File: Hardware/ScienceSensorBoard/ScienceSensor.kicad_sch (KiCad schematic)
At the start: 93 parts, among them J1 Conn_02x03_Counter_Clockwise, J2 RJ45_LED_Shielded, Q1 SI4156DY, Q10 BSS138, Q11 SI4156DY, Q2 SI4156DY, Q3 SI4156DY, Q4 BSS138, Q5 BSS138, Q6 BSS138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

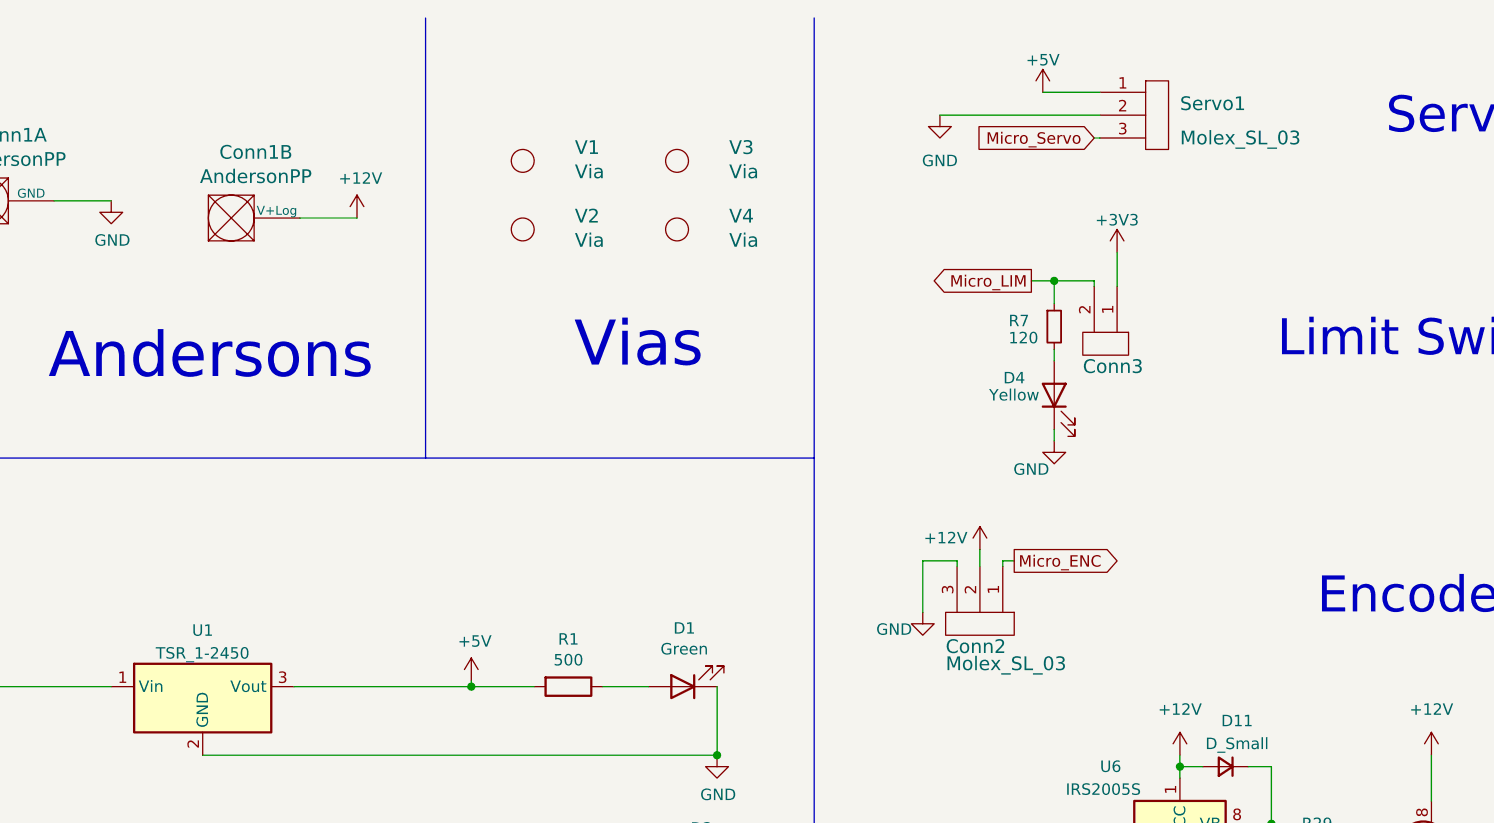
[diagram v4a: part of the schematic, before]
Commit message: Fixing ERC errors, Updated BOM
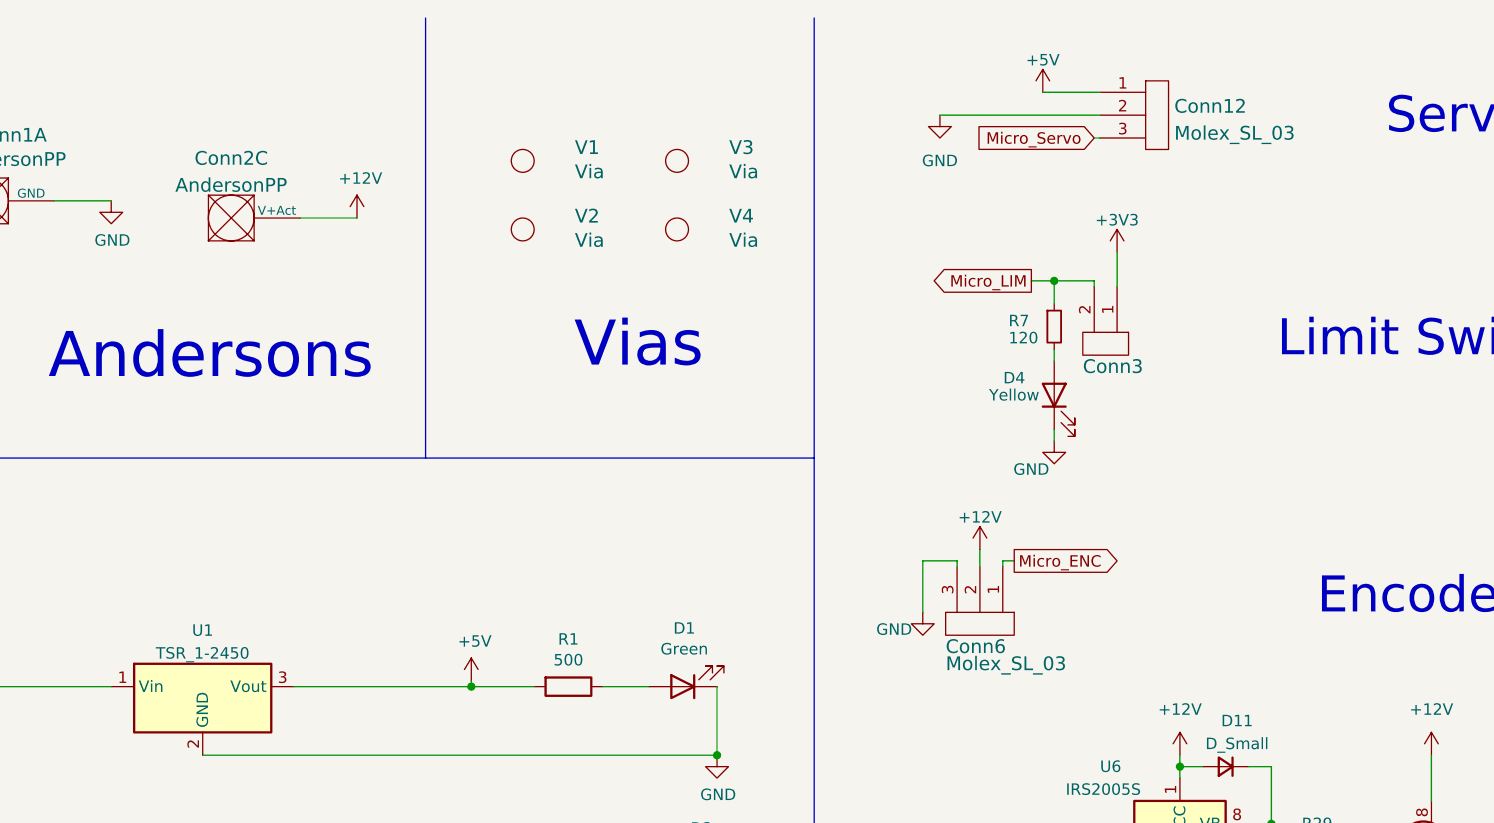
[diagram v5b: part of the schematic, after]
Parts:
- removed unit 2 of Conn1
- added Conn2: AndersonPP, symbol MRDT_Connectors:AndersonPP
- renumbered Servo1 to Conn12, Conn2 to Conn6
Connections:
- net +12V: now also Conn6.2, Conn2.3 (V+Act)
- net +3V3: no longer Conn6.2
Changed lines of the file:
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@@
   (junction (at 254 101.6) (diameter 0) (color 0 0 0 0)
   )
-  (junction (at 264.16 95.25) (diameter 0) (color 0 0 0 0)
-  )
   (junction (at 270.51 217.17) (diameter 0) (color 0 0 0 0)
   )
@@
   (junction (at 216.535 273.685) (diameter 0) (color 0 0 0 0)
   )
+  (junction (at 264.16 95.25) (diameter 0) (color 0 0 0 0)
+  )
   (junction (at 162.56 114.3) (diameter 0) (color 0 0 0 0)
   )
@@
     (stroke (width 0) (type default) (color 0 0 0 0))
   )
+  (wire (pts (xy 264.16 95.25) (xy 264.16 96.52))
+    (stroke (width 0) (type default) (color 0 0 0 0))
+  )
   (wire (pts (xy 53.975 86.36) (xy 73.66 86.36))
     (stroke (width 0) (type default) (color 0 0 0 0))
@@
     (stroke (width 0) (type default) (color 0 0 0 0))
   )
-  (wire (pts (xy 264.16 93.98) (xy 264.16 95.25))
-    (stroke (width 0) (type default) (color 0 0 0 0))
-  )
   (wire (pts (xy 45.085 116.205) (xy 63.5 116.205))
     (stroke (width 0) (type default) (color 0 0 0 0))
@@
     (stroke (width 0) (type default) (color 0 0 0 0))
   )
-  (wire (pts (xy 261.62 95.25) (xy 264.16 95.25))
-    (stroke (width 0) (type default) (color 0 0 0 0))
-  )
   (wire (pts (xy 351.155 156.845) (xy 352.425 156.845))
     (stroke (width 0) (type default) (color 0 0 0 0))
@@
     (stroke (width 0) (type default) (color 0 0 0 0))
   )
+  (wire (pts (xy 264.16 93.98) (xy 264.16 95.25))
+    (stroke (width 0) (type default) (color 0 0 0 0))
+  )
   (wire (pts (xy 277.495 37.465) (xy 277.495 36.83))
     (stroke (width 0) (type default) (color 0 0 0 0))
@@
     (stroke (width 0) (type default) (color 0 0 0 0))
   )
+  (wire (pts (xy 261.62 95.25) (xy 264.16 95.25))
+    (stroke (width 0) (type default) (color 0 0 0 0))
+  )
   (wire (pts (xy 251.46 214.63) (xy 251.46 217.17))
     (stroke (width 0) (type default) (color 0 0 0 0))
@@
     (stroke (width 0) (type default) (color 0 0 0 0))
   )
-  (wire (pts (xy 130.175 71.12) (xy 130.175 73.025))
-    (stroke (width 0) (type default) (color 0 0 0 0))
-  )
   (wire (pts (xy 254 101.6) (xy 254 95.25))
     (stroke (width 0) (type default) (color 0 0 0 0))
@@
     (stroke (width 0) (type default) (color 0 0 0 0))
   )
+  (wire (pts (xy 130.175 71.12) (xy 130.175 73.025))
+    (stroke (width 0) (type default) (color 0 0 0 0))
+  )
   (wire (pts (xy 180.34 109.22) (xy 180.34 110.49))
     (stroke (width 0) (type default) (color 0 0 0 0))
@@
     (stroke (width 0) (type default) (color 0 0 0 0))
   )
-  (wire (pts (xy 264.16 95.25) (xy 264.16 96.52))
-    (stroke (width 0) (type default) (color 0 0 0 0))
-  )
   (wire (pts (xy 97.155 189.23) (xy 97.155 193.04))
     (stroke (width 0) (type default) (color 0 0 0 0))
@@
     (pin "1")
   )
-  (symbol (lib_id "MRDT_Connectors:AndersonPP") (at 44.45 36.83 0) (unit 2)
-    (in_bom yes) (on_board yes)
-    (property "Reference" "Conn1" (id 0) (at 49.7332 27.0002 0)
-      (effects (font (size 1.524 1.524)))
-    )
-    (property "Value" "AndersonPP" (id 1) (at 49.7332 29.6926 0)
-      (effects (font (size 1.524 1.524)))
-    )
-    (property "Footprint" "" (id 2) (at 40.64 50.8 0)
-      (effects (font (size 1.524 1.524)) hide)
-    )
-    (property "Datasheet" "" (id 3) (at 40.64 50.8 0)
-      (effects (font (size 1.524 1.524)) hide)
-    )
-    (pin "1")
-    (pin "2")
-    (pin "3")
-    (pin "4")
-    (pin "1")
-  )
   (symbol (lib_id "power:+5V") (at 73.66 85.725 0) (unit 1)
     (in_bom yes) (on_board yes)
@@
     (pin "VUSB")
   )
-  (symbol (lib_id "ArmBoard_Hardware-rescue:+3.3V-power") (at 130.175 71.12 0) (unit 1)
-    (in_bom yes) (on_board yes)
-    (property "Reference" "#PWR015" (id 0) (at 130.175 74.93 0)
-      (effects (font (size 1.27 1.27)) hide)
-    )
-    (property "Value" "+12V" (id 1) (at 126.365 69.85 0))
-    (property "Footprint" "" (id 2) (at 130.175 71.12 0)
-      (effects (font (size 1.27 1.27)) hide)
-    )
-    (property "Datasheet" "" (id 3) (at 130.175 71.12 0)
-      (effects (font (size 1.27 1.27)) hide)
-    )
-    (pin "1")
-  )
   (symbol (lib_id "power:+5V") (at 370.205 55.245 0) (unit 1)
     (in_bom yes) (on_board yes)
@@
     (pin "1")
   )
+  (symbol (lib_id "power:+12V") (at 130.175 71.12 0) (unit 1)
+    (in_bom yes) (on_board yes) (fields_autoplaced)
+    (property "Reference" "#PWR0101" (id 0) (at 130.175 74.93 0)
+      (effects (font (size 1.27 1.27)) hide)
+    )
+    (property "Value" "+12V" (id 1) (at 130.175 67.5442 0))
+    (property "Footprint" "" (id 2) (at 130.175 71.12 0)
+      (effects (font (size 1.27 1.27)) hide)
+    )
+    (property "Datasheet" "" (id 3) (at 130.175 71.12 0)
+      (effects (font (size 1.27 1.27)) hide)
+    )
+    (pin "1")
+  )
   (symbol (lib_id "MRDT_Connectors:Molex_SL_03") (at 126.365 78.105 270) (unit 1)
     (in_bom yes) (on_board yes)
-    (property "Reference" "Conn2" (id 0) (at 126.365 81.915 90)
+    (property "Reference" "Conn6" (id 0) (at 126.365 81.915 90)
       (effects (font (size 1.524 1.524)) (justify left))
     )
@@
     (pin "2")
   )
+  (symbol (lib_id "MRDT_Connectors:AndersonPP") (at 44.45 36.83 0) (unit 3)
+    (in_bom yes) (on_board yes) (fields_autoplaced)
+    (property "Reference" "Conn2" (id 0) (at 46.99 27.6659 0)
+      (effects (font (size 1.524 1.524)))
+    )
+    (property "Value" "AndersonPP" (id 1) (at 46.99 30.6593 0)
+      (effects (font (size 1.524 1.524)))
+    )
+    (property "Footprint" "" (id 2) (at 40.64 50.8 0)
+      (effects (font (size 1.524 1.524)) hide)
+    )
+    (property "Datasheet" "" (id 3) (at 40.64 50.8 0)
+      (effects (font (size 1.524 1.524)) hide)
+    )
+    (pin "1")
+    (pin "2")
+    (pin "3")
+    (pin "4")
+    (pin "1")
+  )
   (symbol (lib_id "power:+5V") (at 81.28 179.07 0) (unit 1)
     (in_bom yes) (on_board yes)
@@
   (symbol (lib_id "MRDT_Connectors:Molex_SL_03") (at 148.59 26.67 0) (unit 1)
     (in_bom yes) (on_board yes) (fields_autoplaced)
-    (property "Reference" "Servo1" (id 0) (at 152.4 21.59 0)
+    (property "Reference" "Conn12" (id 0) (at 151.765 21.8838 0)
       (effects (font (size 1.524 1.524)) (justify left))
     )
-    (property "Value" "Molex_SL_03" (id 1) (at 152.4 25.4 0)
+    (property "Value" "Molex_SL_03" (id 1) (at 151.765 24.8772 0)
       (effects (font (size 1.524 1.524)) (justify left))
     )
@@
       (reference "#PWR014") (unit 1) (value "GND") (footprint "")
     )
-    (path "/2fa72ae1-4629-4bfe-ba46-42c110783f4a"
-      (reference "#PWR015") (unit 1) (value "+12V") (footprint "")
-    )
     (path "/2cd81dea-5dd1-45c5-97bb-42b6bc72e149"
       (reference "#PWR016") (unit 1) (value "+5V") (footprint "")
@@
       (reference "#PWR067") (unit 1) (value "GND") (footprint "")
     )
+    (path "/49671190-4e1a-4b03-a0e9-4da1774c1d67"
+      (reference "#PWR0101") (unit 1) (value "+12V") (footprint "")
+    )
     (path "/7becaed6-99a4-49f3-99dd-3fce229dac4a"
       (reference "C1") (unit 1) (value "0.1uF") (footprint "Capacitor_SMD:C_0603_1608Metric_Pad1.08x0.95mm_HandSolder")
@@
       (reference "Conn1") (unit 1) (value "AndersonPP") (footprint "")
     )
-    (path "/00000000-0000-0000-0000-000063214fb6"
-      (reference "Conn1") (unit 2) (value "AndersonPP") (footprint "")
-    )
-    (path "/514d1d3a-5e7e-4cdf-800d-dc9fd4979572"
-      (reference "Conn2") (unit 1) (value "Molex_SL_03") (footprint "MRDT_Connectors:MOLEX_SL_03_Vertical")
+    (path "/7095feda-30c9-4bfd-9ce4-1857ac5357e8"
+      (reference "Conn2") (unit 3) (value "AndersonPP") (footprint "")
     )
     (path "/362043ba-7077-4355-842f-ed4e21c764a7"
@@
       (reference "Conn5") (unit 2) (value "AndersonPP") (footprint "MRDT_Connectors:Anderson_2_Horizontal_Side_by_Side")
     )
+    (path "/514d1d3a-5e7e-4cdf-800d-dc9fd4979572"
+      (reference "Conn6") (unit 1) (value "Molex_SL_03") (footprint "MRDT_Connectors:MOLEX_SL_03_Vertical")
+    )
     (path "/0801cfcf-c1b0-4c18-945f-084fcc49db23"
       (reference "Conn7") (unit 1) (value "Molex_SL_03") (footprint "")
@@
       (reference "Conn11") (unit 1) (value "Molex_SL_04") (footprint "MRDT_Connectors:MOLEX_SL_04_Horizontal")
     )
+    (path "/c7884a03-c37f-45a7-baa0-a34c76a7670d"
+      (reference "Conn12") (unit 1) (value "Molex_SL_03") (footprint "")
+    )
     (path "/00000000-0000-0000-0000-000063231caf"
       (reference "D1") (unit 1) (value "Green") (footprint "")
@@
       (reference "R34") (unit 1) (value "100") (footprint "Resistor_SMD:R_0603_1608Metric_Pad0.98x0.95mm_HandSolder")
     )
-    (path "/c7884a03-c37f-45a7-baa0-a34c76a7670d"
-      (reference "Servo1") (unit 1) (value "Molex_SL_03") (footprint "")
-    )
     (path "/c5bc5e0f-59b7-45b6-b17c-1888cdf8bc2c"

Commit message: LED breakout, sensor changes
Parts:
- removed C3, C6: 2.2uF, Capacitor_SMD:C_0603_1608Metric_Pad1.08x0.95mm_HandSolder, symbol Device:C
- removed C5, C7: 3.3nF, Capacitor_SMD:C_0603_1608Metric_Pad1.08x0.95mm_HandSolder, symbol Device:C
- removed Conn11: Molex_SL_04, MRDT_Connectors:MOLEX_SL_04_Horizontal, symbol MRDT_Connectors:Molex_SL_04
- removed Conn4: Molex_SL_05, symbol MRDT_Connectors:Molex_SL_05
- removed R20, R26: 56k, Resistor_SMD:R_0603_1608Metric_Pad0.98x0.95mm_HandSolder, symbol Device:R
- removed R21, R27: 1M, Resistor_SMD:R_0603_1608Metric_Pad0.98x0.95mm_HandSolder, symbol Device:R
- removed U4, U5: TSV911RILT, Package_TO_SOT_SMD:SOT-23-5, symbol Amplifier_Operational:TSV911RILT
- added Conn4: Molex_SL_07, symbol MRDT_Connectors:Molex_SL_07
- added Conn?: Molex_SL_04, symbol MRDT_Connectors:Molex_SL_04
- added D? (x3): Blue, symbol Device:LED
- added R?: 100, symbol Device:R
- added R? (x2): 500, symbol Device:R
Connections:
- net +12V: now also Conn4.1
- net +5V: now also Conn4.2, Conn?.1
- net GND: now also Conn4.3, Conn?.2, D?.1 (K), D?.1 (K), D?.1 (K)
- net LED_315: now reaches U3.17 (A3)
- net LED_315: now also Conn4.7, R?.2
- net CH4_TX: now reaches U3.28 (RX7)
- net CH4_TX: now also Conn?.3, R?.2
- net CH4_RX: now reaches U3.29 (TX7)
- net CH4_RX: now also Conn?.4, R?.2
- net LED_1 renamed LED_260
- net LED_260: now also Conn4.4
- net LED_2 renamed LED_275
- net LED_275: now also Conn4.5
- net LED_3 renamed LED_280
- net LED_280: now also Conn4.6
- net NO_Gas: no longer names the net of U3.41 (A17)
- net NO_Ref: no longer names the net of U3.40 (A16)
- new net: D?.2 (A), R?.1 (x3)
- no-connect marks 41 -> 40
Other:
- note added: "CH4_Sensor"
- note removed: "NO_Sensor"
- moved on the sheet: Conn10, Conn8, Conn9, D10, D3, D5, D6, D7, D8, D9, Q7, R12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

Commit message: NH3, LED Mosfets
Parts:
- added Conn?: Molex_SL_04, symbol MRDT_Connectors:Molex_SL_04
- added R?: 820, symbol Device:R
- added R?: 93.1, symbol Device:R
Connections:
- net +5V: now also Conn?.1, Conn?.2; no longer Conn4.2
- net GND: now also Conn4.2, R?.1, R?.1; no longer Conn4.3
- net Micro_ENC: now also U3.40 (A16); no longer U3.27 (A13)
- net Micro_FWD: now also U3.38 (A14); no longer U3.25 (A11)
- net Micro_LIM: now also U3.41 (A17); no longer U3.38 (A14)
- net Micro_RVS: now also U3.27 (A13); no longer U3.24 (A10)
- net Micro_Servo: now also U3.39 (A15); no longer U3.26 (A12)
- net Photodiode_1: no longer U3.23 (A9)
- net NH3: now reaches U3.22 (A8)
- net NH3: now also Conn?.4, R?.2
- new net: Conn?.3, R?.2
- new net Photodiode_260: U3.26 (A12)
- new net Photodiode_275: U3.25 (A11)
- new net Photodiode_280: U3.24 (A10)
- new net Photodiode_315: U3.23 (A9)
- no-connect marks 40 -> 37
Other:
- note added: "NH3_Sensor"

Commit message: Footprint Assignment
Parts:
- added R36: 330, Resistor_SMD:R_0603_1608Metric_Pad0.98x0.95mm_HandSolder, symbol Device:R
- C10, C8: footprint Capacitor_SMD:C_0603_1608Metric -> Capacitor_SMD:C_0603_1608Metric_Pad1.08x0.95mm_HandSolder
- C2, C4, C9: footprint (none) -> Capacitor_SMD:C_0603_1608Metric_Pad1.08x0.95mm_HandSolder
- Conn1, Conn2: footprint (none) -> MRDT_Connectors:Anderson_2_Horizontal_Side_by_Side
- Conn11, Conn13: renamed from Conn?; footprint (none) -> MRDT_Connectors:MOLEX_SL_04_Vertical
- Conn12, Conn7: footprint (none) -> MRDT_Connectors:MOLEX_SL_03_Vertical
- Conn4: footprint (none) -> MRDT_Connectors:MOLEX_SL_07_Vertical
- Conn8, Conn9: footprint (none) -> MRDT_Connectors:MOLEX_SL_04_Vertical
- D1, D10, D12, D13, D2, D3, D5, D6, D7, D8, D9: footprint (none) -> LED_SMD:LED_0603_1608Metric_Pad1.05x0.95mm_HandSolder
- D11, D14: footprint (none) -> Diode_SMD:D_0603_1608Metric_Pad1.05x0.95mm_HandSolder
- D15, D16, D17: renamed from D?; footprint (none) -> LED_SMD:LED_0603_1608Metric_Pad1.05x0.95mm_HandSolder
- Q10, Q4, Q5, Q6, Q7, Q8, Q9: footprint (none) -> Package_TO_SOT_SMD:SOT-323_SC-70_Handsoldering
- R1, R10, R11, R12, R13, R14, R15, R16, R17, R18, R19, R2, R22, R23, R24, R25, R28, R3, R4, R5, R6, R8, R9: footprint (none) -> Resistor_SMD:R_0603_1608Metric_Pad0.98x0.95mm_HandSolder
- R20, R21, R26, R27: renamed from R?; footprint (none) -> Resistor_SMD:R_0603_1608Metric_Pad0.98x0.95mm_HandSolder
- R35: renamed from R?; value 820 -> 510; footprint (none) -> Resistor_SMD:R_0603_1608Metric_Pad0.98x0.95mm_HandSolder
- V1, V2, V3, V4: footprint (none) -> MRDT_Drill_Holes:Via_.6mm
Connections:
- net +3V3: now also Conn13.2
- net +5V: no longer Conn13.2
- net GND: now also R36.1; no longer R35.1
- new net: R35.1, R36.2
- no-connect marks 37 -> 40
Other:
- moved on the sheet: R27, R35
